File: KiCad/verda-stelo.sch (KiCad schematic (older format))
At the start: 91 parts, among them U1 74HC595

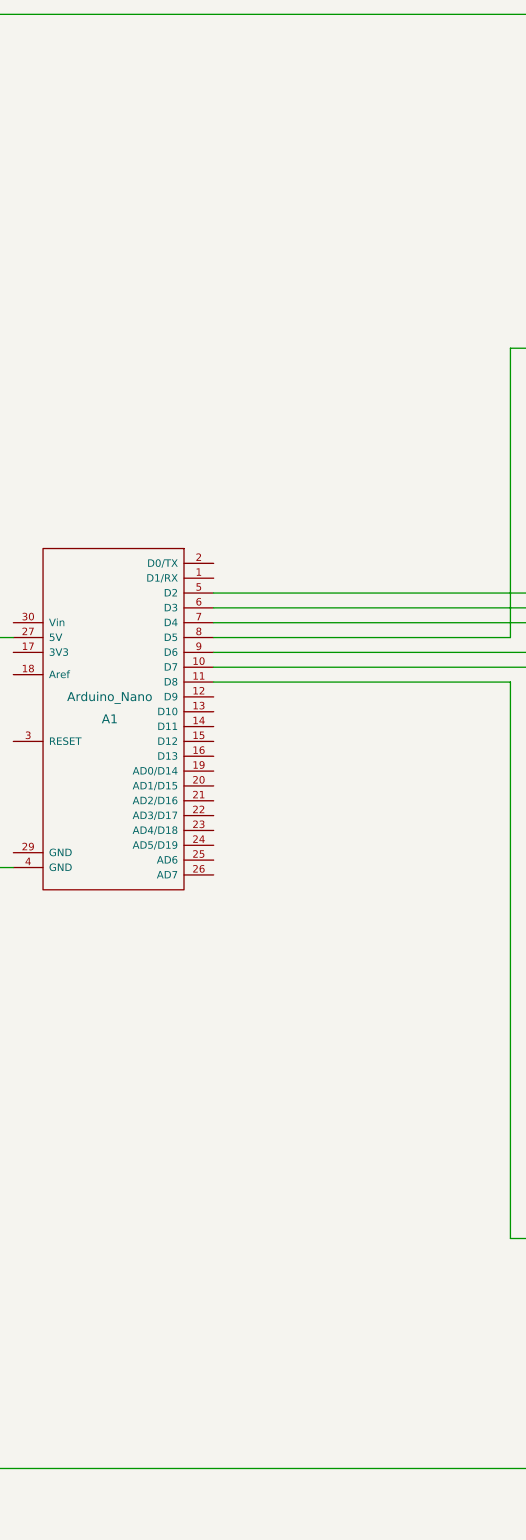
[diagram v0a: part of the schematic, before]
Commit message: Add button to change drivers
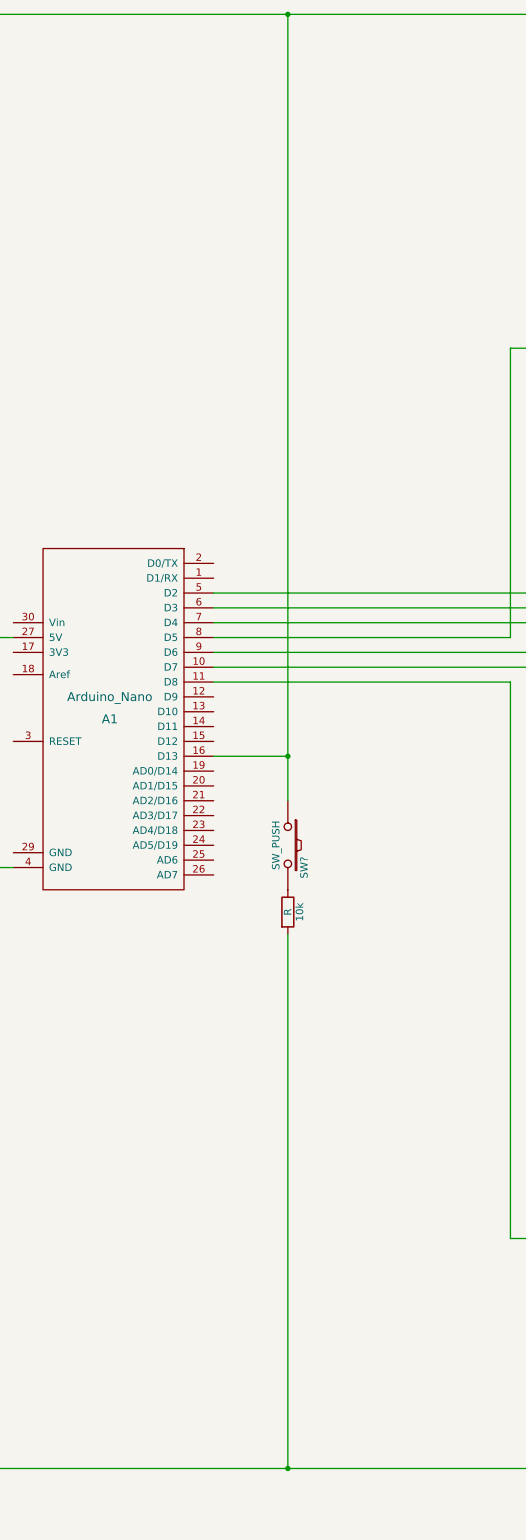
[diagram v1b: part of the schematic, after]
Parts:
- added 10k: R, symbol R
- added SW?: SW_PUSH, symbol SW_PUSH
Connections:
- net GND: now also 10k.2
- net VCC: now also A1.16 (D13), SW?.1
- new net: 10k.1, SW?.2
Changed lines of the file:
@@
 LIBS:contrib
 LIBS:valves
-LIBS:arduino_nano
 LIBS:verda-stelo-cache
 EELAYER 25 0
@@
 	10500 2600 5400 2600
 Connection ~ 5400 2600
+$Comp
+L R 10k
+U 1 1 5A5234D5
+P 2900 6850
+F 0 "10k" V 2980 6850 50  0000 C CNN
+F 1 "R" V 2900 6850 50  0000 C CNN
+F 2 "" V 2830 6850 50  0000 C CNN
+F 3 "" H 2900 6850 50  0000 C CNN
+	1    2900 6850
+	1    0    0    -1
+$EndComp
+Wire Wire Line
+	2900 7000 2900 10600
+Connection ~ 2900 10600
+$Comp
+L SW_PUSH SW?
+U 1 1 5A5239D5
+P 2900 6400
+F 0 "SW?" H 3050 6510 50  0000 C CNN
+F 1 "SW_PUSH" H 2900 6320 50  0000 C CNN
+F 2 "" H 2900 6400 50  0000 C CNN
+F 3 "" H 2900 6400 50  0000 C CNN
+	1    2900 6400
+	0    1    1    0
+$EndComp
+Wire Wire Line
+	2400 5800 2900 5800
+Wire Wire Line
+	2900 800  2900 6100
+Connection ~ 2900 800
+Connection ~ 2900 5800
 $EndSCHEMATC
